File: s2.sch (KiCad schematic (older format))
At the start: 49 parts, among them J3 phones, J4 MIC_PTT, K2 FRT5, K3 FRT5, Q1 MMBT2222LT1G, Q2 BC847, U6 NE5532

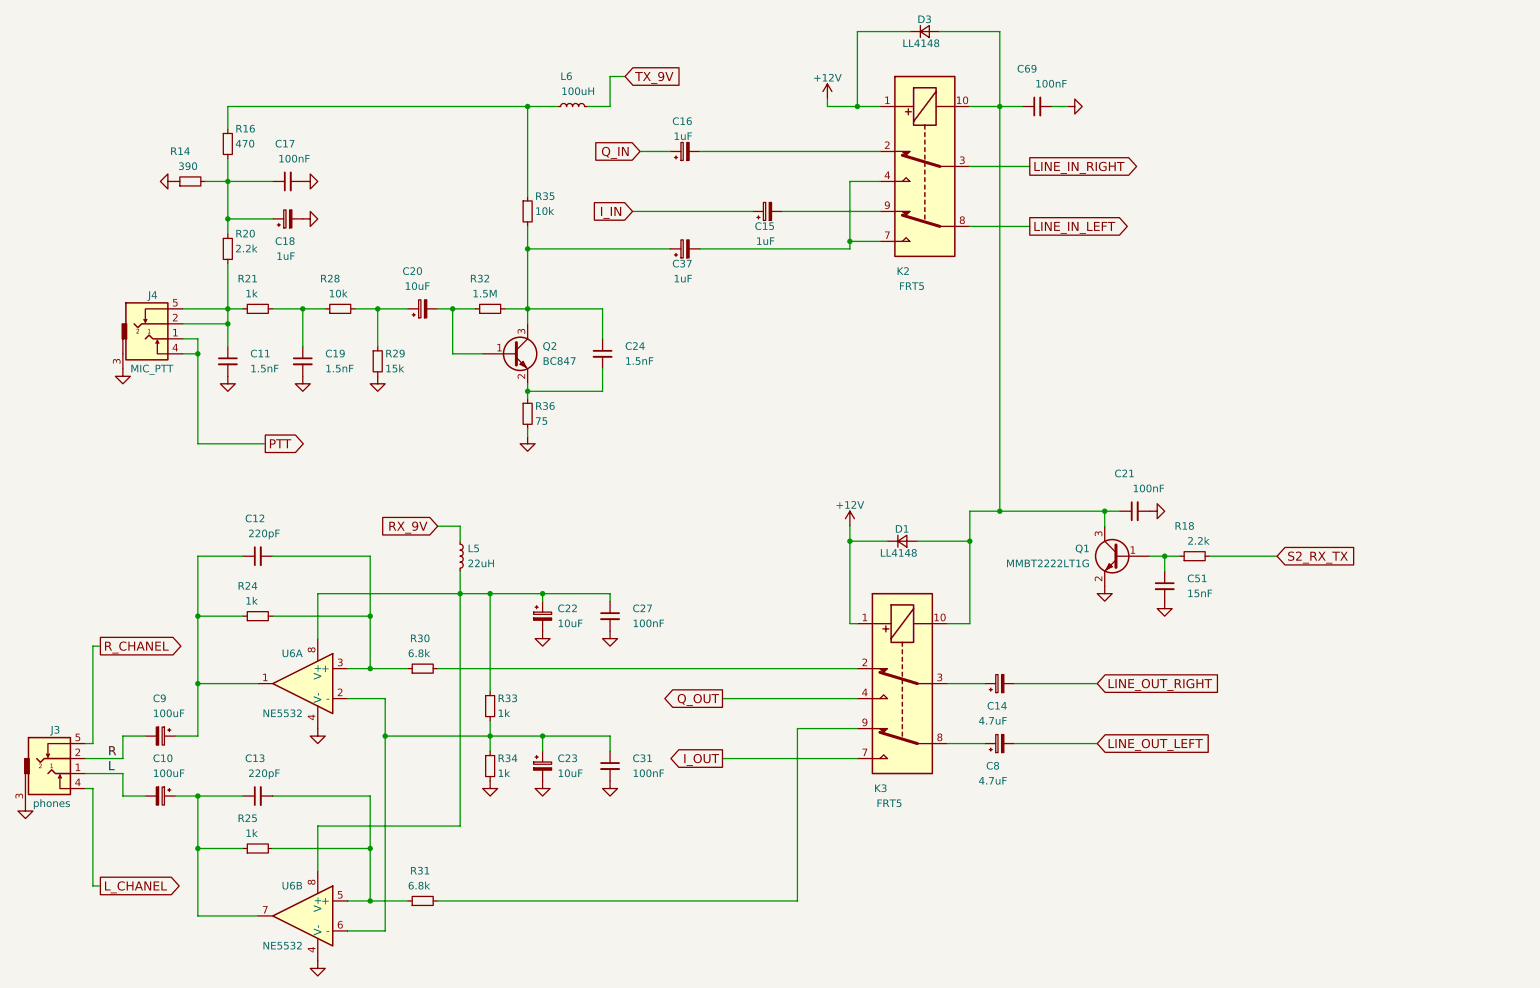
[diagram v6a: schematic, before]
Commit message: PCB 74LCX574
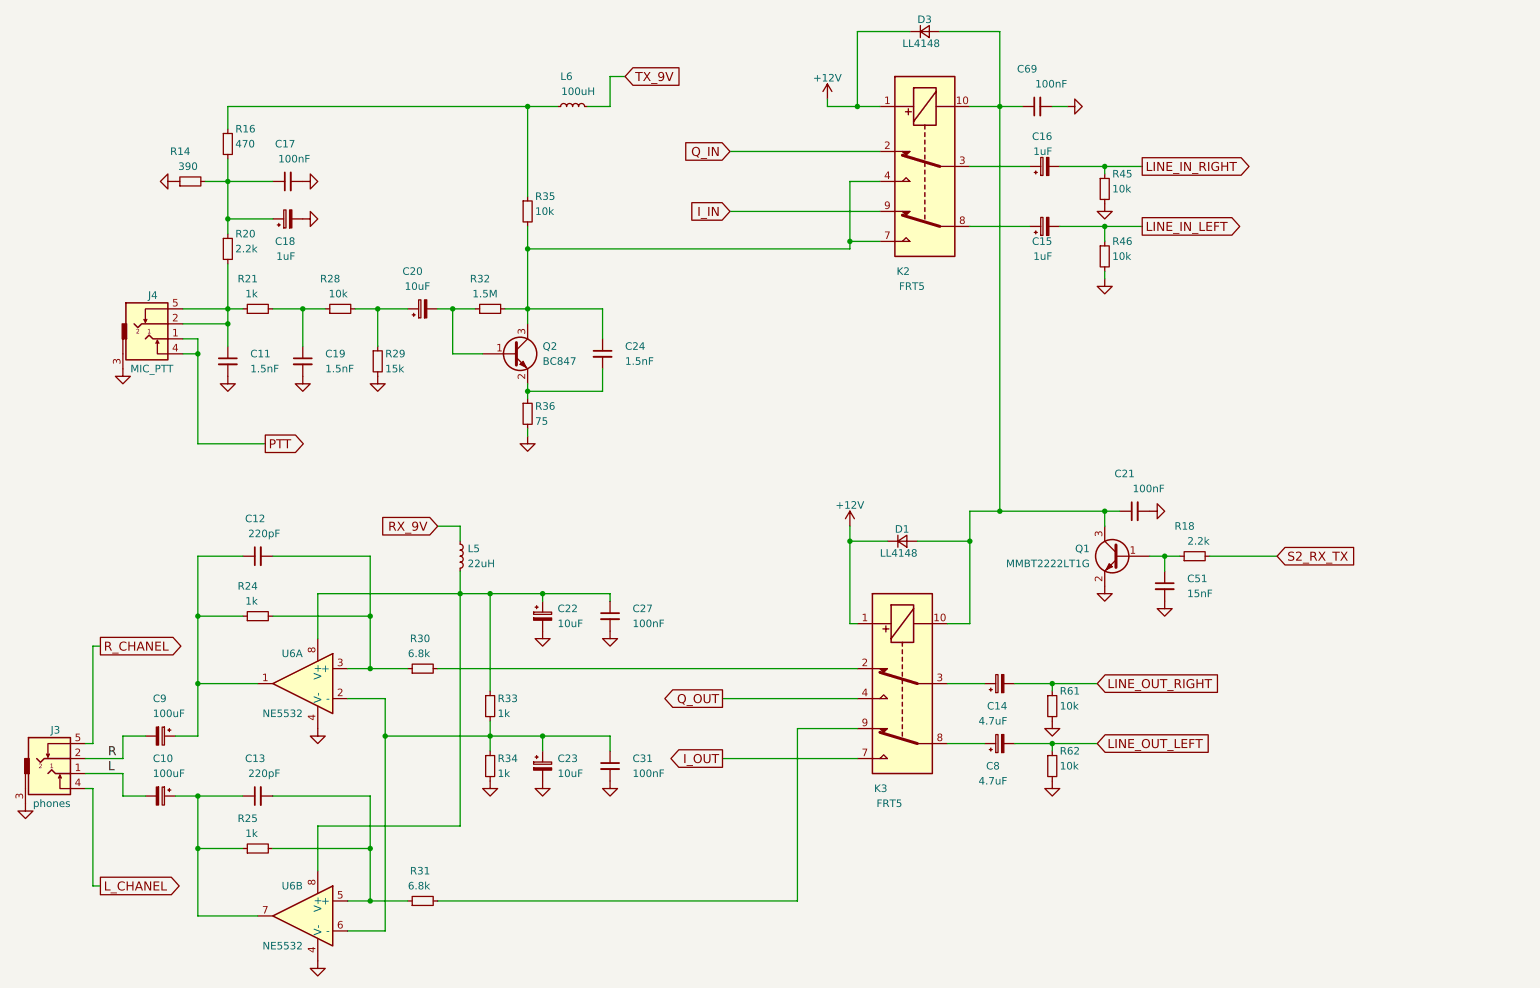
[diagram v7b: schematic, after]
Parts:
- removed C37: 1uF, Capacitors_THT:CP_Radial_D5.0mm_P2.00mm, symbol CP_Small
- added R45, R46, R61, R62: 10k, UI:R_1206_0603, symbol R_Small
- C15, C16: footprint Capacitors_Tantalum_SMD:CP_Tantalum_Case-A_EIA-3216-18_Wave -> Capacitors_THT:CP_Radial_D5.0mm_P2.00mm
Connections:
- net GND: now also R45.2, R46.2, R61.2, R62.2
- net I_IN: now also K2.9; no longer C15.1
- net LINE_IN_LEFT: now also C15.2, R46.1; no longer K2.8
- net LINE_IN_RIGHT: now also C16.2, R45.1; no longer K2.3
- net LINE_OUT_LEFT: now also R62.1
- net LINE_OUT_RIGHT: now also R61.1
- net Q_IN: now also K2.2; no longer C16.1
- net at C24.1, Q2.3 (C), R32.2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: now also K2.4, K2.7
- new net: C15.1, K2.8
- new net: C16.1, K2.3
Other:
- moved on the sheet: C15, C16
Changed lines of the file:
@@
 $Descr A4 11693 8268
 encoding utf-8
-Sheet 6 7
+Sheet 5 7
 Title ""
 Date ""
@@
 Comment4 ""
 $EndDescr
-Text GLabel 7550 2000 2    60   Output ~ 0
+Text GLabel 8300 2000 2    60   Output ~ 0
 LINE_IN_LEFT
-Text GLabel 7550 1600 2    60   Output ~ 0
+Text GLabel 8300 1600 2    60   Output ~ 0
 LINE_IN_RIGHT
-Text GLabel 4900 1900 0    60   Input ~ 0
+Text GLabel 5550 1900 0    60   Input ~ 0
 I_IN
-Text GLabel 4950 1500 0    60   Input ~ 0
+Text GLabel 5550 1500 0    60   Input ~ 0
 Q_IN
 $Comp
-L GND #PWR66
+L GND #PWR68
 U 1 1 5DE7E3AF
 P 8050 4400
-F 0 "#PWR66" H 8050 4150 50  0001 C CNN
+F 0 "#PWR68" H 8050 4150 50  0001 C CNN
 F 1 "GND" H 8050 4250 50  0001 C CNN
 F 2 "" H 8050 4400 50  0001 C CNN
@@
 $EndComp
 $Comp
-L GND #PWR67
+L GND #PWR69
 U 1 1 5DE7E3B9
 P 8350 3900
-F 0 "#PWR67" H 8350 3650 50  0001 C CNN
+F 0 "#PWR69" H 8350 3650 50  0001 C CNN
 F 1 "GND" H 8350 3750 50  0001 C CNN
 F 2 "" H 8350 3900 50  0001 C CNN
@@
 $EndComp
 $Comp
-L GND #PWR68
+L GND #PWR70
 U 1 1 5DE7E3DB
 P 8450 4500
-F 0 "#PWR68" H 8450 4250 50  0001 C CNN
+F 0 "#PWR70" H 8450 4250 50  0001 C CNN
 F 1 "GND" H 8450 4350 50  0001 C CNN
 F 2 "" H 8450 4500 50  0001 C CNN
@@
 L CP_Small C15
 U 1 1 5DE7ED0D
-P 5800 1900
-F 0 "C15" V 5700 1850 50  0000 L CNN
-F 1 "1uF" V 5600 1850 50  0000 L CNN
-F 2 "Capacitors_Tantalum_SMD:CP_Tantalum_Case-A_EIA-3216-18_Wave" H 5800 1900 50  0001 C CNN
-F 3 "" H 5800 1900 50  0001 C CNN
-	1    5800 1900
+P 7650 2000
+F 0 "C15" V 7550 1950 50  0000 L CNN
+F 1 "1uF" V 7450 1950 50  0000 L CNN
+F 2 "Capacitors_THT:CP_Radial_D5.0mm_P2.00mm" H 7650 2000 50  0001 C CNN
+F 3 "" H 7650 2000 50  0001 C CNN
+	1    7650 2000
 	0    -1   -1   0
 $EndComp
@@
 L CP_Small C16
 U 1 1 5DE7EDD4
-P 5250 1500
-F 0 "C16" V 5450 1450 50  0000 L CNN
-F 1 "1uF" V 5350 1450 50  0000 L CNN
-F 2 "Capacitors_Tantalum_SMD:CP_Tantalum_Case-A_EIA-3216-18_Wave" H 5250 1500 50  0001 C CNN
-F 3 "" H 5250 1500 50  0001 C CNN
-	1    5250 1500
+P 7650 1600
+F 0 "C16" V 7850 1550 50  0000 L CNN
+F 1 "1uF" V 7750 1550 50  0000 L CNN
+F 2 "Capacitors_THT:CP_Radial_D5.0mm_P2.00mm" H 7650 1600 50  0001 C CNN
+F 3 "" H 7650 1600 50  0001 C CNN
+	1    7650 1600
 	0    -1   -1   0
 $EndComp
@@
 	7150 1600 7550 1600
 Wire Wire Line
-	4950 1500 5150 1500
-Wire Wire Line
-	4900 1900 5700 1900
+	5550 1500 6550 1500
+Wire Wire Line
+	5550 1900 6550 1900
 Text GLabel 8000 5450 2    60   Input ~ 0
 LINE_OUT_LEFT
@@
 Wire Wire Line
 	5500 5550 6400 5550
-Wire Wire Line
-	5350 1500 6550 1500
 $Comp
 L L_Small L6
@@
 	4200 3050 4200 3150
 $Comp
-L GND #PWR58
+L GND #PWR56
 U 1 1 5EA8447C
 P 4200 3400
-F 0 "#PWR58" H 4200 3150 50  0001 C CNN
+F 0 "#PWR56" H 4200 3150 50  0001 C CNN
 F 1 "GND" H 4200 3250 50  0001 C CNN
 F 2 "" H 4200 3400 50  0001 C CNN
@@
 Wire Wire Line
 	3700 2850 3900 2850
-$Comp
-L CP_Small C37
-U 1 1 5EA859D6
-P 5250 2150
-F 0 "C37" V 5150 2100 50  0000 L CNN
-F 1 "1uF" V 5050 2100 50  0000 L CNN
-F 2 "Capacitors_THT:CP_Radial_D5.0mm_P2.00mm" H 5250 2150 50  0001 C CNN
-F 3 "" H 5250 2150 50  0001 C CNN
-	1    5250 2150
-	0    -1   -1   0
-$EndComp
-Wire Wire Line
-	6350 2150 5350 2150
-Wire Wire Line
-	5150 2150 4200 2150
+Wire Wire Line
+	6350 2150 4200 2150
 Connection ~ 3700 2550
 $Comp
@@
 	3050 2550 3400 2550
 $Comp
-L GND #PWR56
+L GND #PWR54
 U 1 1 5EA86A3F
 P 3200 3000
-F 0 "#PWR56" H 3200 2750 50  0001 C CNN
+F 0 "#PWR54" H 3200 2750 50  0001 C CNN
 F 1 "GND" H 3200 2850 50  0001 C CNN
 F 2 "" H 3200 3000 50  0001 C CNN
@@
 Connection ~ 2700 2550
 $Comp
-L GND #PWR53
+L GND #PWR51
 U 1 1 5EA87223
 P 2700 3000
-F 0 "#PWR53" H 2700 2750 50  0001 C CNN
+F 0 "#PWR51" H 2700 2750 50  0001 C CNN
 F 1 "GND" H 2700 2850 50  0001 C CNN
 F 2 "" H 2700 3000 50  0001 C CNN
@@
 Connection ~ 2200 2650
 $Comp
-L GND #PWR48
+L GND #PWR46
 U 1 1 5EA87A28
 P 1500 2950
-F 0 "#PWR48" H 1500 2700 50  0001 C CNN
+F 0 "#PWR46" H 1500 2700 50  0001 C CNN
 F 1 "GND" H 1500 2800 50  0001 C CNN
 F 2 "" H 1500 2950 50  0001 C CNN
@@
 $EndComp
 $Comp
-L GND #PWR50
+L GND #PWR48
 U 1 1 5EA87D5A
 P 2200 3000
-F 0 "#PWR50" H 2200 2750 50  0001 C CNN
+F 0 "#PWR48" H 2200 2750 50  0001 C CNN
 F 1 "GND" H 2200 2850 50  0001 C CNN
 F 2 "" H 2200 3000 50  0001 C CNN
@@
 $EndComp
 $Comp
-L GND #PWR52
+L GND #PWR50
 U 1 1 5EA88DC1
 P 2700 1950
-F 0 "#PWR52" H 2700 1700 50  0001 C CNN
+F 0 "#PWR50" H 2700 1700 50  0001 C CNN
 F 1 "GND" H 2700 1800 50  0001 C CNN
 F 2 "" H 2700 1950 50  0001 C CNN
@@
 $EndComp
 $Comp
-L GND #PWR51
+L GND #PWR49
 U 1 1 5EA88EC8
 P 2700 1700
-F 0 "#PWR51" H 2700 1450 50  0001 C CNN
+F 0 "#PWR49" H 2700 1450 50  0001 C CNN
 F 1 "GND" H 2700 1550 50  0001 C CNN
 F 2 "" H 2700 1700 50  0001 C CNN
@@
 	2200 1350 2200 1200
 $Comp
-L GND #PWR49
+L GND #PWR47
 U 1 1 5EA8A2B0
 P 1850 1700
-F 0 "#PWR49" H 1850 1450 50  0001 C CNN
+F 0 "#PWR47" H 1850 1450 50  0001 C CNN
 F 1 "GND" H 1850 1550 50  0001 C CNN
 F 2 "" H 1850 1700 50  0001 C CNN
@@
 Connection ~ 3950 5400
 $Comp
-L GND #PWR57
+L GND #PWR55
 U 1 1 5EA8DADD
 P 3950 5700
-F 0 "#PWR57" H 3950 5450 50  0001 C CNN
+F 0 "#PWR55" H 3950 5450 50  0001 C CNN
 F 1 "GND" H 3950 5550 50  0001 C CNN
 F 2 "" H 3950 5700 50  0001 C CNN
@@
 $EndComp
 $Comp
-L GND #PWR60
+L GND #PWR58
 U 1 1 5EA9039E
 P 4300 5700
-F 0 "#PWR60" H 4300 5450 50  0001 C CNN
+F 0 "#PWR58" H 4300 5450 50  0001 C CNN
 F 1 "GND" H 4300 5550 50  0001 C CNN
 F 2 "" H 4300 5700 50  0001 C CNN
@@
 $EndComp
 $Comp
-L GND #PWR62
+L GND #PWR60
 U 1 1 5EA91527
 P 4750 5700
-F 0 "#PWR62" H 4750 5450 50  0001 C CNN
+F 0 "#PWR60" H 4750 5450 50  0001 C CNN
 F 1 "GND" H 4750 5550 50  0001 C CNN
 F 2 "" H 4750 5700 50  0001 C CNN
@@
 	1500 5800 1650 5800
 $Comp
-L GND #PWR54
+L GND #PWR52
 U 1 1 5EA93E43
 P 2800 5350
-F 0 "#PWR54" H 2800 5100 50  0001 C CNN
+F 0 "#PWR52" H 2800 5100 50  0001 C CNN
 F 1 "GND" H 2800 5200 50  0001 C CNN
 F 2 "" H 2800 5350 50  0001 C CNN
@@
 $EndComp
 $Comp
-L GND #PWR55
+L GND #PWR53
 U 1 1 5EA93F05
 P 2800 6900
-F 0 "#PWR55" H 2800 6650 50  0001 C CNN
+F 0 "#PWR53" H 2800 6650 50  0001 C CNN
 F 1 "GND" H 2800 6750 50  0001 C CNN
 F 2 "" H 2800 6900 50  0001 C CNN
@@
 $EndComp
 $Comp
-L GND #PWR47
+L GND #PWR45
 U 1 1 5EA94135
 P 850 5850
-F 0 "#PWR47" H 850 5600 50  0001 C CNN
+F 0 "#PWR45" H 850 5600 50  0001 C CNN
 F 1 "GND" H 850 5700 50  0001 C CNN
 F 2 "" H 850 5850 50  0001 C CNN
@@
 Connection ~ 4300 4450
 $Comp
-L GND #PWR59
+L GND #PWR57
 U 1 1 5EA94B85
 P 4300 4700
-F 0 "#PWR59" H 4300 4450 50  0001 C CNN
+F 0 "#PWR57" H 4300 4450 50  0001 C CNN
 F 1 "GND" H 4300 4550 50  0001 C CNN
 F 2 "" H 4300 4700 50  0001 C CNN
@@
 $EndComp
 $Comp
-L GND #PWR61
+L GND #PWR59
 U 1 1 5EA94C4D
 P 4750 4700
-F 0 "#PWR61" H 4750 4450 50  0001 C CNN
+F 0 "#PWR59" H 4750 4450 50  0001 C CNN
 F 1 "GND" H 4750 4550 50  0001 C CNN
 F 2 "" H 4750 4700 50  0001 C CNN
@@
 	1    0    0    -1
 $EndComp
-Wire Wire Line
-	5900 1900 6550 1900
 Wire Wire Line
 	6350 1700 6350 2150
@@
 $EndComp
 Wire Wire Line
-	8050 4000 8050 3900
+	8050 3900 8050 4000
 Wire Wire Line
 	7150 3900 8150 3900
@@
 	7150 4650 7000 4650
 $Comp
-L +12V #PWR64
+L +12V #PWR62
 U 1 1 5EB0655B
 P 6350 4000
-F 0 "#PWR64" H 6350 3850 50  0001 C CNN
+F 0 "#PWR62" H 6350 3850 50  0001 C CNN
 F 1 "+12V" H 6350 4140 50  0000 C CNN
 F 2 "" H 6350 4000 50  0001 C CNN
@@
 	7700 1200 7800 1200
 $Comp
-L +12V #PWR63
+L +12V #PWR61
 U 1 1 5EB364C9
 P 6200 1150
-F 0 "#PWR63" H 6200 1000 50  0001 C CNN
+F 0 "#PWR61" H 6200 1000 50  0001 C CNN
 F 1 "+12V" H 6200 1290 50  0000 C CNN
 F 2 "" H 6200 1150 50  0001 C CNN
@@
 Text GLabel 2450 3450 2    60   Output ~ 0
 PTT
+Wire Wire Line
+	7750 1600 8300 1600
+Wire Wire Line
+	7750 2000 8300 2000
+$Comp
+L R_Small R46
+U 1 1 5EDB25F8
+P 8050 2200
+F 0 "R46" H 8100 2300 50  0000 L CNN
+F 1 "10k" H 8100 2200 50  0000 L CNN
+F 2 "UI:R_1206_0603" H 8050 2200 50  0001 C CNN
+F 3 "" H 8050 2200 50  0001 C CNN
+	1    8050 2200
+	1    0    0    -1
+$EndComp
+$Comp
+L GND #PWR67
+U 1 1 5EDB28D4
+P 8050 2350
+F 0 "#PWR67" H 8050 2100 50  0001 C CNN
+F 1 "GND" H 8050 2200 50  0001 C CNN
+F 2 "" H 8050 2350 50  0001 C CNN
+F 3 "" H 8050 2350 50  0001 C CNN
+	1    8050 2350
+	1    0    0    -1
+$EndComp
+Wire Wire Line
+	8050 2300 8050 2350
+Wire Wire Line
+	8050 2100 8050 2000
+Connection ~ 8050 2000
+$Comp
+L R_Small R45
+U 1 1 5EDB2D1C
+P 8050 1750
+F 0 "R45" H 8100 1850 50  0000 L CNN
+F 1 "10k" H 8100 1750 50  0000 L CNN
+F 2 "UI:R_1206_0603" H 8050 1750 50  0001 C CNN
+F 3 "" H 8050 1750 50  0001 C CNN
+	1    8050 1750
+	1    0    0    -1
+$EndComp
+$Comp
+L GND #PWR66
+U 1 1 5EDB2DD9
+P 8050 1850
+F 0 "#PWR66" H 8050 1600 50  0001 C CNN
+F 1 "GND" H 8050 1700 50  0001 C CNN
+F 2 "" H 8050 1850 50  0001 C CNN
+F 3 "" H 8050 1850 50  0001 C CNN
+	1    8050 1850
+	1    0    0    -1
+$EndComp
+Wire Wire Line
+	8050 1650 8050 1600
+Connection ~ 8050 1600
+$Comp
+L R_Small R61
+U 1 1 5EDB6325
+P 7700 5200
+F 0 "R61" H 7750 5300 50  0000 L CNN
+F 1 "10k" H 7750 5200 50  0000 L CNN
+F 2 "UI:R_1206_0603" H 7700 5200 50  0001 C CNN
+F 3 "" H 7700 5200 50  0001 C CNN
+	1    7700 5200
+	1    0    0    -1
+$EndComp
+$Comp
+L GND #PWR63
+U 1 1 5EDB6895
+P 7700 5300
+F 0 "#PWR63" H 7700 5050 50  0001 C CNN
+F 1 "GND" H 7700 5150 50  0001 C CNN
+F 2 "" H 7700 5300 50  0001 C CNN
+F 3 "" H 7700 5300 50  0001 C CNN
+	1    7700 5300
+	1    0    0    -1
+$EndComp
+$Comp
+L R_Small R62
+U 1 1 5EDB6A0C
+P 7700 5600
+F 0 "R62" H 7750 5700 50  0000 L CNN
+F 1 "10k" H 7750 5600 50  0000 L CNN
+F 2 "UI:R_1206_0603" H 7700 5600 50  0001 C CNN
+F 3 "" H 7700 5600 50  0001 C CNN
+	1    7700 5600
+	1    0    0    -1
+$EndComp
+$Comp
+L GND #PWR64
+U 1 1 5EDB6AC7
+P 7700 5700
+F 0 "#PWR64" H 7700 5450 50  0001 C CNN
+F 1 "GND" H 7700 5550 50  0001 C CNN
+F 2 "" H 7700 5700 50  0001 C CNN
+F 3 "" H 7700 5700 50  0001 C CNN
+	1    7700 5700
+	1    0    0    -1
+$EndComp
+Wire Wire Line
+	7700 5500 7700 5450
+Connection ~ 7700 5450
+Wire Wire Line
+	7700 5100 7700 5050
+Connection ~ 7700 5050
 $EndSCHEMATC
